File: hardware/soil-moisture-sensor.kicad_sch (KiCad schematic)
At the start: 35 parts, among them J1 USB_B_Micro, Q1 Q_NPN_BEC, Q2 Q_NPN_BEC, SW1 SW_Push, SW2 SW_Push, U2 CP2102N-Axx-xQFN24, U3 ESP32-WROOM-32D

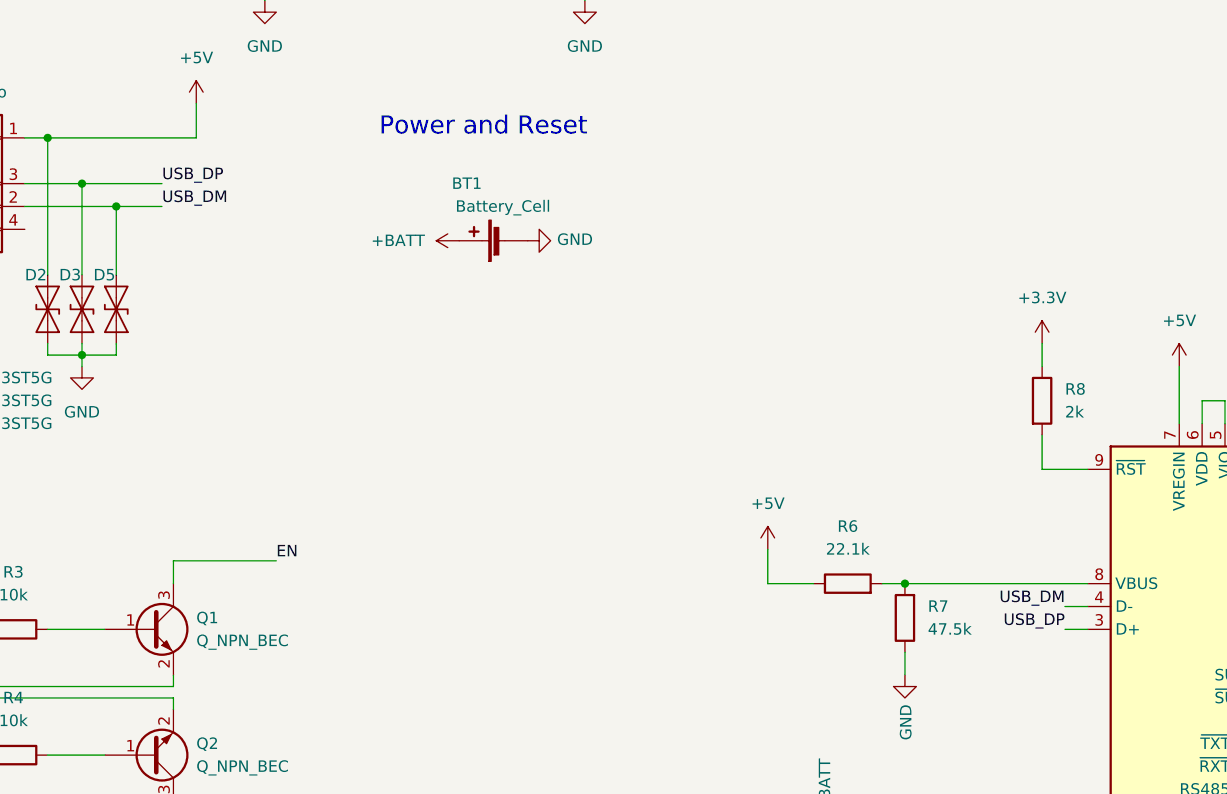
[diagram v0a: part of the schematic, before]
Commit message: updated cr123a fp
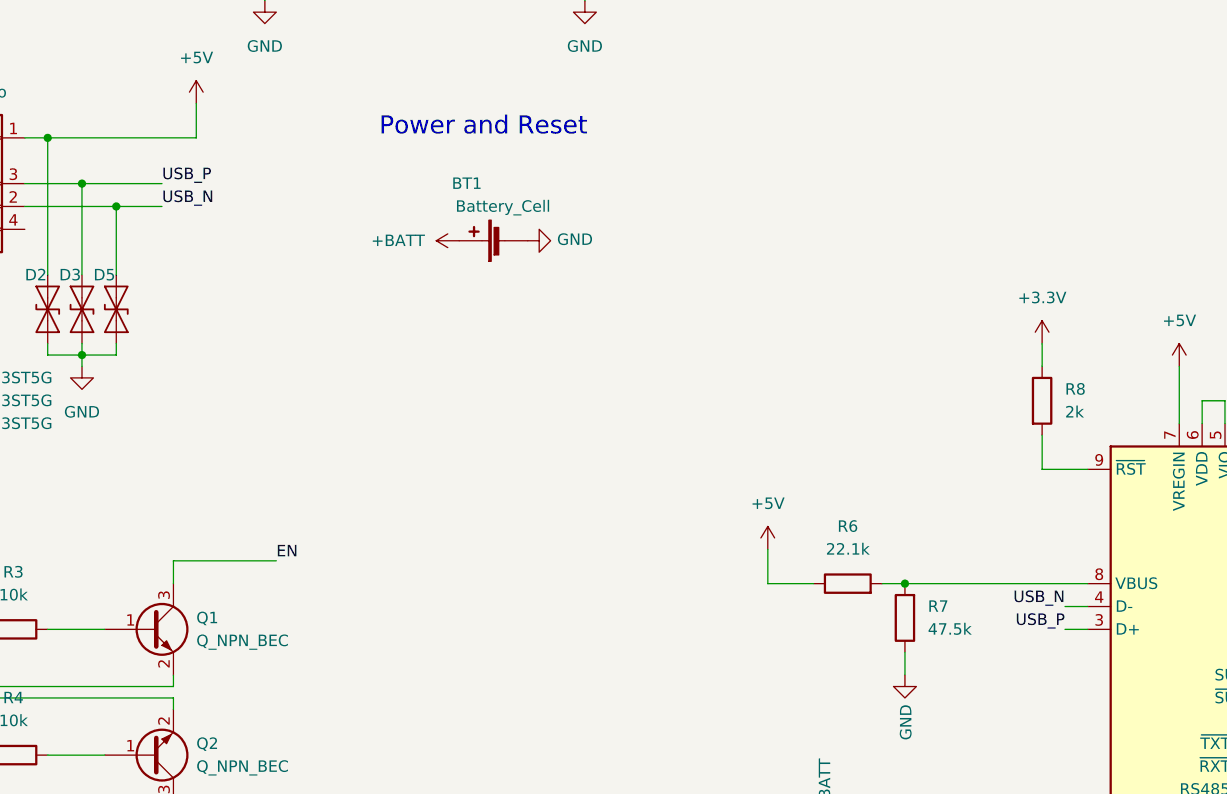
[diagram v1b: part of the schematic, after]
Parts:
- R1: footprint (none) -> Resistor_SMD:R_0603_1608Metric
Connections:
- net USB_DM renamed USB_N
- net USB_DP renamed USB_P
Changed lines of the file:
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@@
     (effects (font (size 1.27 1.27)) (justify left bottom))
   )
-  (label "USB_DM" (at 52.07 82.55 0)
+  (label "USB_N" (at 52.07 82.55 0)
     (effects (font (size 1.27 1.27)) (justify left bottom))
   )
@@
     (effects (font (size 1.27 1.27)) (justify left bottom))
   )
-  (label "USB_DP" (at 152.4 129.54 180)
+  (label "USB_P" (at 152.4 129.54 180)
     (effects (font (size 1.27 1.27)) (justify right bottom))
   )
@@
     (effects (font (size 1.27 1.27)) (justify left bottom))
   )
-  (label "USB_DP" (at 52.07 80.01 0)
+  (label "USB_P" (at 52.07 80.01 0)
     (effects (font (size 1.27 1.27)) (justify left bottom))
   )
@@
     (effects (font (size 1.27 1.27)) (justify left bottom))
   )
-  (label "USB_DM" (at 152.4 127 180)
+  (label "USB_N" (at 152.4 127 180)
     (effects (font (size 1.27 1.27)) (justify right bottom))
   )
@@
       (effects (font (size 1.27 1.27)) (justify left))
     )
-    (property "Footprint" "" (id 2) (at 41.91 168.402 90)
+    (property "Footprint" "Resistor_SMD:R_0603_1608Metric" (id 2) (at 41.91 168.402 90)
       (effects (font (size 1.27 1.27)) hide)
     )

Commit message: layout finished
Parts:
- removed D1: D_Schottky, Diode_SMD:D_SOD-323_HandSoldering, symbol Device:D_Schottky
- BT1: footprint kicad_footprints:CR123A Battery Holder -> (none)
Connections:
- net +3V3 is gone; now on an unnamed net: D10.2 (A), D9.2 (A), R8.1
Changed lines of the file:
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@@
   (junction (at 30.48 143.51) (diameter 0) (color 0 0 0 0)
   )
-  (junction (at 67.31 170.18) (diameter 0) (color 0 0 0 0)
-  )
   (junction (at 172.72 66.04) (diameter 0) (color 0 0 0 0)
   )
-  (junction (at 59.69 170.18) (diameter 0) (color 0 0 0 0)
-  )
   (junction (at 120.65 48.26) (diameter 0) (color 0 0 0 0)
   )
@@
   (junction (at 29.21 129.54) (diameter 0) (color 0 0 0 0)
   )
+  (junction (at 170.18 92.71) (diameter 0) (color 0 0 0 0)
+  )
   (junction (at 99.06 54.61) (diameter 0) (color 0 0 0 0)
   )
@@
   (junction (at 53.34 170.18) (diameter 0) (color 0 0 0 0)
   )
+  (junction (at 170.18 104.14) (diameter 0) (color 0 0 0 0)
+  )
   (junction (at 46.99 82.55) (diameter 0) (color 0 0 0 0)
   )
@@
     (stroke (width 0) (type default) (color 0 0 0 0))
   )
+  (wire (pts (xy 191.77 120.65) (xy 191.77 92.71))
+    (stroke (width 0) (type default) (color 0 0 0 0))
+  )
   (wire (pts (xy 72.39 175.26) (xy 72.39 170.18))
     (stroke (width 0) (type default) (color 0 0 0 0))
@@
     (stroke (width 0) (type default) (color 0 0 0 0))
   )
+  (wire (pts (xy 149.86 92.71) (xy 170.18 92.71))
+    (stroke (width 0) (type default) (color 0 0 0 0))
+  )
   (wire (pts (xy 43.18 97.79) (xy 43.18 99.06))
     (stroke (width 0) (type default) (color 0 0 0 0))
@@
     (stroke (width 0) (type default) (color 0 0 0 0))
   )
+  (wire (pts (xy 191.77 92.71) (xy 170.18 92.71))
+    (stroke (width 0) (type default) (color 0 0 0 0))
+  )
+  (wire (pts (xy 149.86 92.71) (xy 149.86 100.33))
+    (stroke (width 0) (type default) (color 0 0 0 0))
+  )
   (wire (pts (xy 63.5 54.61) (xy 63.5 48.26))
     (stroke (width 0) (type default) (color 0 0 0 0))
@@
     (stroke (width 0) (type default) (color 0 0 0 0))
   )
-  (wire (pts (xy 149.86 97.79) (xy 149.86 100.33))
-    (stroke (width 0) (type default) (color 0 0 0 0))
-  )
   (wire (pts (xy 29.21 137.16) (xy 53.34 137.16))
     (stroke (width 0) (type default) (color 0 0 0 0))
@@
     (stroke (width 0) (type default) (color 0 0 0 0))
   )
+  (wire (pts (xy 226.06 120.65) (xy 191.77 120.65))
+    (stroke (width 0) (type default) (color 0 0 0 0))
+  )
   (wire (pts (xy 99.06 54.61) (xy 99.06 48.26))
     (stroke (width 0) (type default) (color 0 0 0 0))
@@
     (stroke (width 0) (type default) (color 0 0 0 0))
   )
+  (wire (pts (xy 170.18 92.71) (xy 170.18 104.14))
+    (stroke (width 0) (type default) (color 0 0 0 0))
+  )
   (wire (pts (xy 67.31 170.18) (xy 72.39 170.18))
     (stroke (width 0) (type default) (color 0 0 0 0))
@@
     (stroke (width 0) (type default) (color 0 0 0 0))
   )
-  (wire (pts (xy 226.06 140.97) (xy 226.06 147.32))
+  (wire (pts (xy 226.06 120.65) (xy 226.06 147.32))
     (stroke (width 0) (type default) (color 0 0 0 0))
   )
@@
     (pin "2")
   )
-  (symbol (lib_id "Device:D_Schottky") (at 63.5 170.18 180) (unit 1)
-    (in_bom yes) (on_board yes)
-    (property "Reference" "D1" (id 0) (at 63.5 164.6682 0))
-    (property "Value" "D_Schottky" (id 1) (at 63.5 166.9796 0))
-    (property "Footprint" "Diode_SMD:D_SOD-323_HandSoldering" (id 2) (at 63.5 170.18 0)
-      (effects (font (size 1.27 1.27)) hide)
-    )
-    (property "Datasheet" "~" (id 3) (at 63.5 170.18 0)
-      (effects (font (size 1.27 1.27)) hide)
-    )
-    (property "LCSC" "C154819" (id 4) (at 63.5 170.18 0)
-      (effects (font (size 1.27 1.27)) hide)
-    )
-    (property "Config" "+rotated" (id 5) (at 63.5 170.18 0)
-      (effects (font (size 1.27 1.27)) hide)
-    )
-    (pin "1")
-    (pin "2")
-  )
   (symbol (lib_id "Device:C") (at 72.39 179.07 0) (unit 1)
     (in_bom yes) (on_board yes)
@@
       (effects (font (size 1.27 1.27)) (justify left))
     )
-    (property "Footprint" "kicad_footprints:CR123A Battery Holder" (id 2) (at 88.646 86.36 90)
+    (property "Footprint" "" (id 2) (at 88.646 86.36 90)
       (effects (font (size 1.27 1.27)) hide)
     )
@@
     )
     (property "Datasheet" "" (id 3) (at 85.09 86.36 0)
-      (effects (font (size 1.27 1.27)) hide)
-    )
-    (pin "1")
-  )
-  (symbol (lib_id "power:+3.3V") (at 149.86 97.79 0) (unit 1)
-    (in_bom yes) (on_board yes) (fields_autoplaced)
-    (property "Reference" "#PWR0109" (id 0) (at 149.86 101.6 0)
-      (effects (font (size 1.27 1.27)) hide)
-    )
-    (property "Value" "+3.3V" (id 1) (at 149.86 92.71 0))
-    (property "Footprint" "" (id 2) (at 149.86 97.79 0)
-      (effects (font (size 1.27 1.27)) hide)
-    )
-    (property "Datasheet" "" (id 3) (at 149.86 97.79 0)
       (effects (font (size 1.27 1.27)) hide)
     )
@@
     (pin "2")
   )
-  (symbol (lib_id "power:+3.3V") (at 226.06 140.97 0) (unit 1)
-    (in_bom yes) (on_board yes) (fields_autoplaced)
-    (property "Reference" "#PWR0121" (id 0) (at 226.06 144.78 0)
-      (effects (font (size 1.27 1.27)) hide)
-    )
-    (property "Value" "+3.3V" (id 1) (at 226.06 135.89 0))
-    (property "Footprint" "" (id 2) (at 226.06 140.97 0)
-      (effects (font (size 1.27 1.27)) hide)
-    )
-    (property "Datasheet" "" (id 3) (at 226.06 140.97 0)
-      (effects (font (size 1.27 1.27)) hide)
-    )
-    (pin "1")
-  )
   (symbol (lib_id "Device:R") (at 125.73 161.29 0) (unit 1)
     (in_bom yes) (on_board yes) (fields_autoplaced)
@@
       (reference "#PWR0108") (unit 1) (value "GND") (footprint "")
     )
-    (path "/0cba82e5-d1e1-437f-82d3-0b9a2b946b20"
-      (reference "#PWR0109") (unit 1) (value "+3.3V") (footprint "")
-    )
     (path "/f1464702-28e1-4165-bc4d-b76870dc525c"
       (reference "#PWR0110") (unit 1) (value "GND") (footprint "")
@@
       (reference "#PWR0120") (unit 1) (value "GND") (footprint "")
     )
-    (path "/7e78ffed-cc11-4b8c-ba2c-b61290137c1b"
-      (reference "#PWR0121") (unit 1) (value "+3.3V") (footprint "")
-    )
     (path "/00000000-0000-0000-0000-00005f29204b"
       (reference "BT1") (unit 1) (value "Battery_Cell") (footprint "kicad_footprints:CR123A Battery Holder")
@@
       (reference "C7") (unit 1) (value "0.1uF") (footprint "Capacitor_SMD:C_0603_1608Metric")
     )
-    (path "/00000000-0000-0000-0000-00005f25c560"
-      (reference "D1") (unit 1) (value "D_Schottky") (footprint "Diode_SMD:D_SOD-323_HandSoldering")
-    )
     (path "/dd9e85a2-1701-4185-a52a-41467f6ec144"

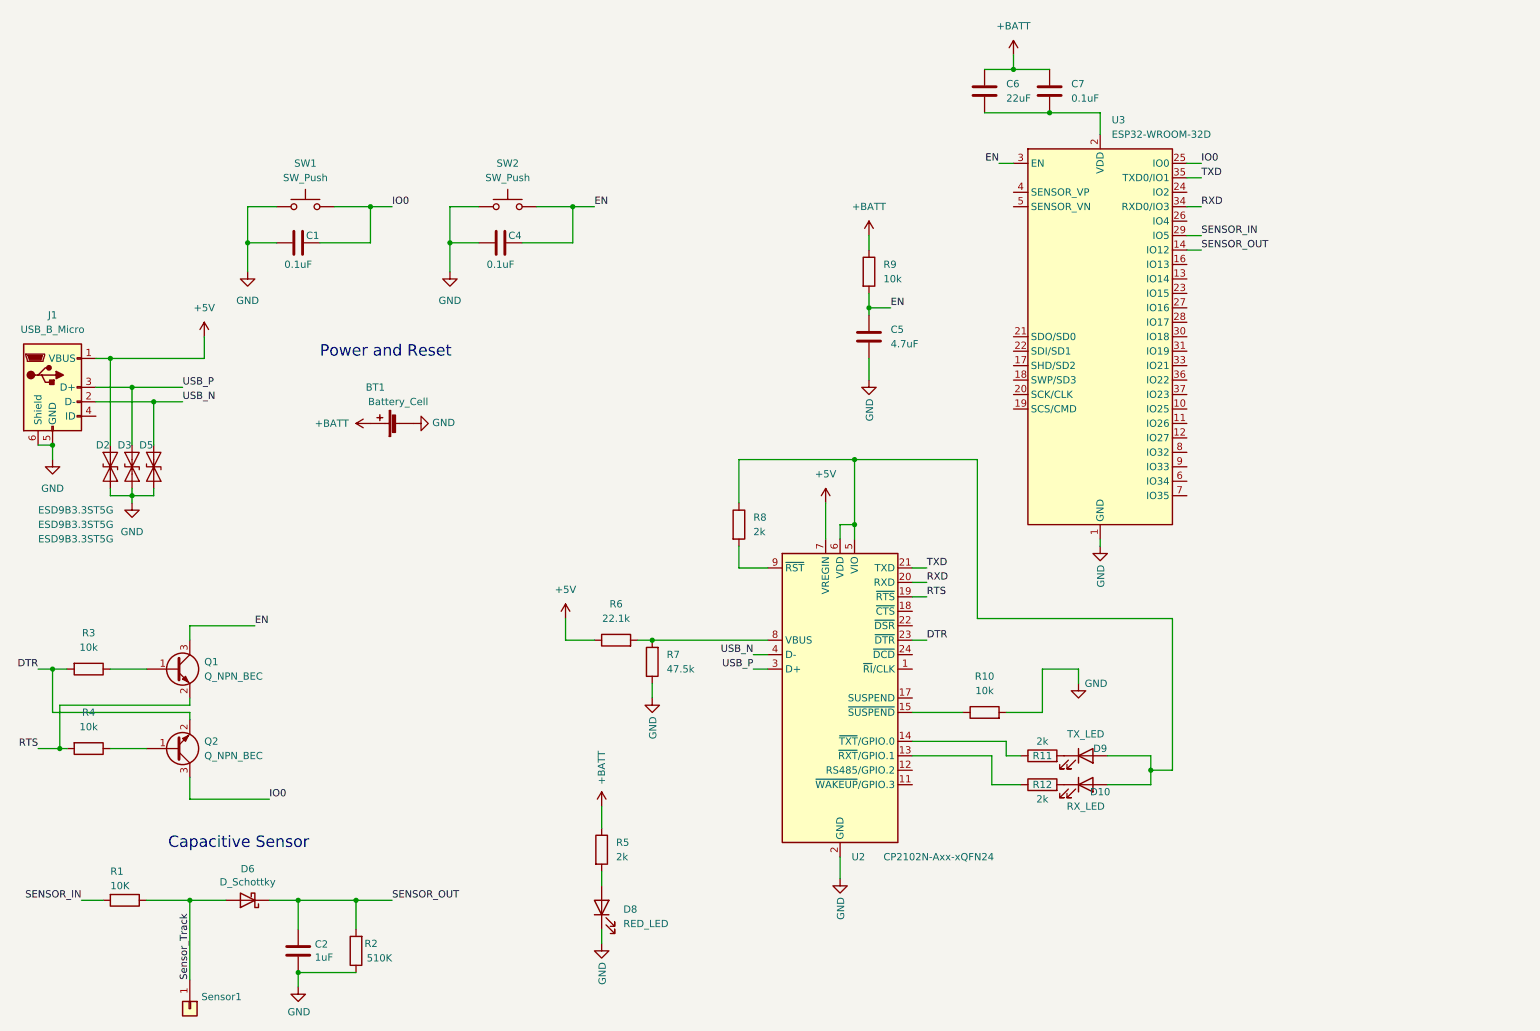
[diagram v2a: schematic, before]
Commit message: removed esd diodes, changed sensor out to adc pin
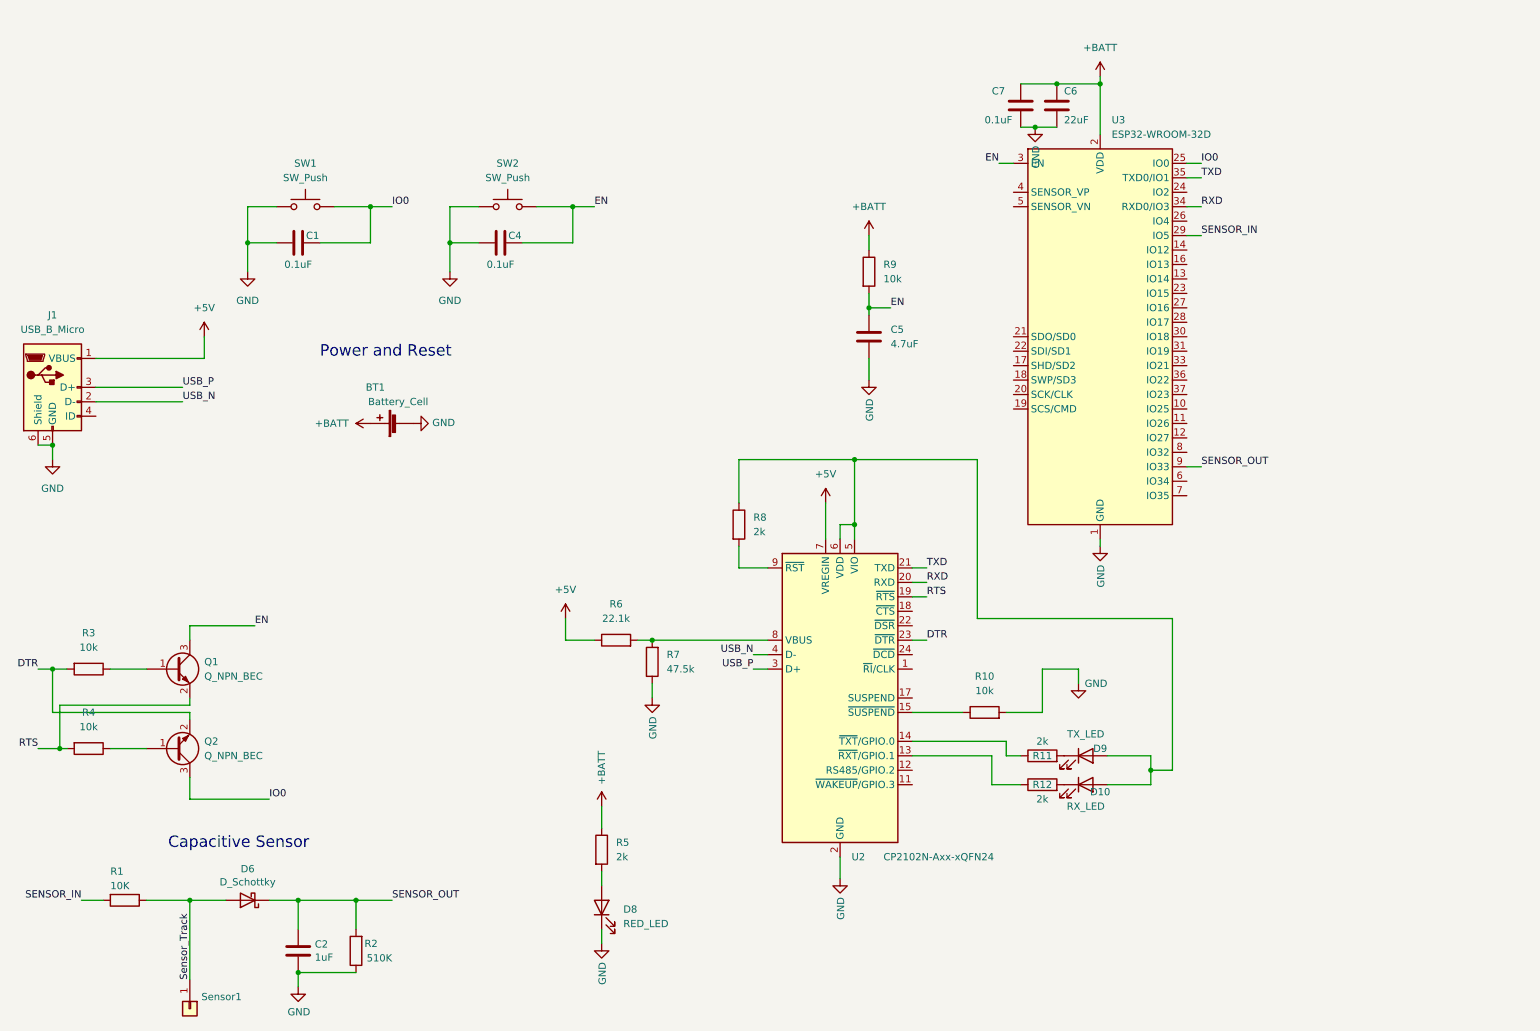
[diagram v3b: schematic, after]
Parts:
- removed D2, D3, D5: ESD9B3.3ST5G, Diode_SMD:D_SOD-923, symbol Diode:ESD9B3.3ST5G
- BT1: footprint (none) -> kicad_footprints:CR123A Battery Holder
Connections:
- net +BATT: now also U3.2 (VDD)
- net GND: now also C6.2, C7.2
- net SENSOR_OUT: now also U3.9 (IO33); no longer U3.14 (IO12)
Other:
- moved on the sheet: C6, C7
